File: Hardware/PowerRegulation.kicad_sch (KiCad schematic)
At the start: 43 parts, among them Q3 AO3401A, U13 TPS54332DDA, U14 AMS1117-3.3, U15 RT9193-33GB, U8 STUSB4500QTR

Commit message: further clean up, switch to desktop
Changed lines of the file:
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@@
 		(end 170.18 190.5)
 		(stroke
-			(width 0.254)
+			(width 0.1778)
 			(type solid)
 		)
@@
 	(text "Indicator LEDs\n"
 		(exclude_from_sim no)
-		(at 204.216 23.622 0)
+		(at 203.454 23.622 0)
 		(effects
 			(font
@@
 	(text "Testpoints"
 		(exclude_from_sim no)
-		(at 205.74 73.66 0)
+		(at 200.152 73.66 0)
 		(effects
 			(font

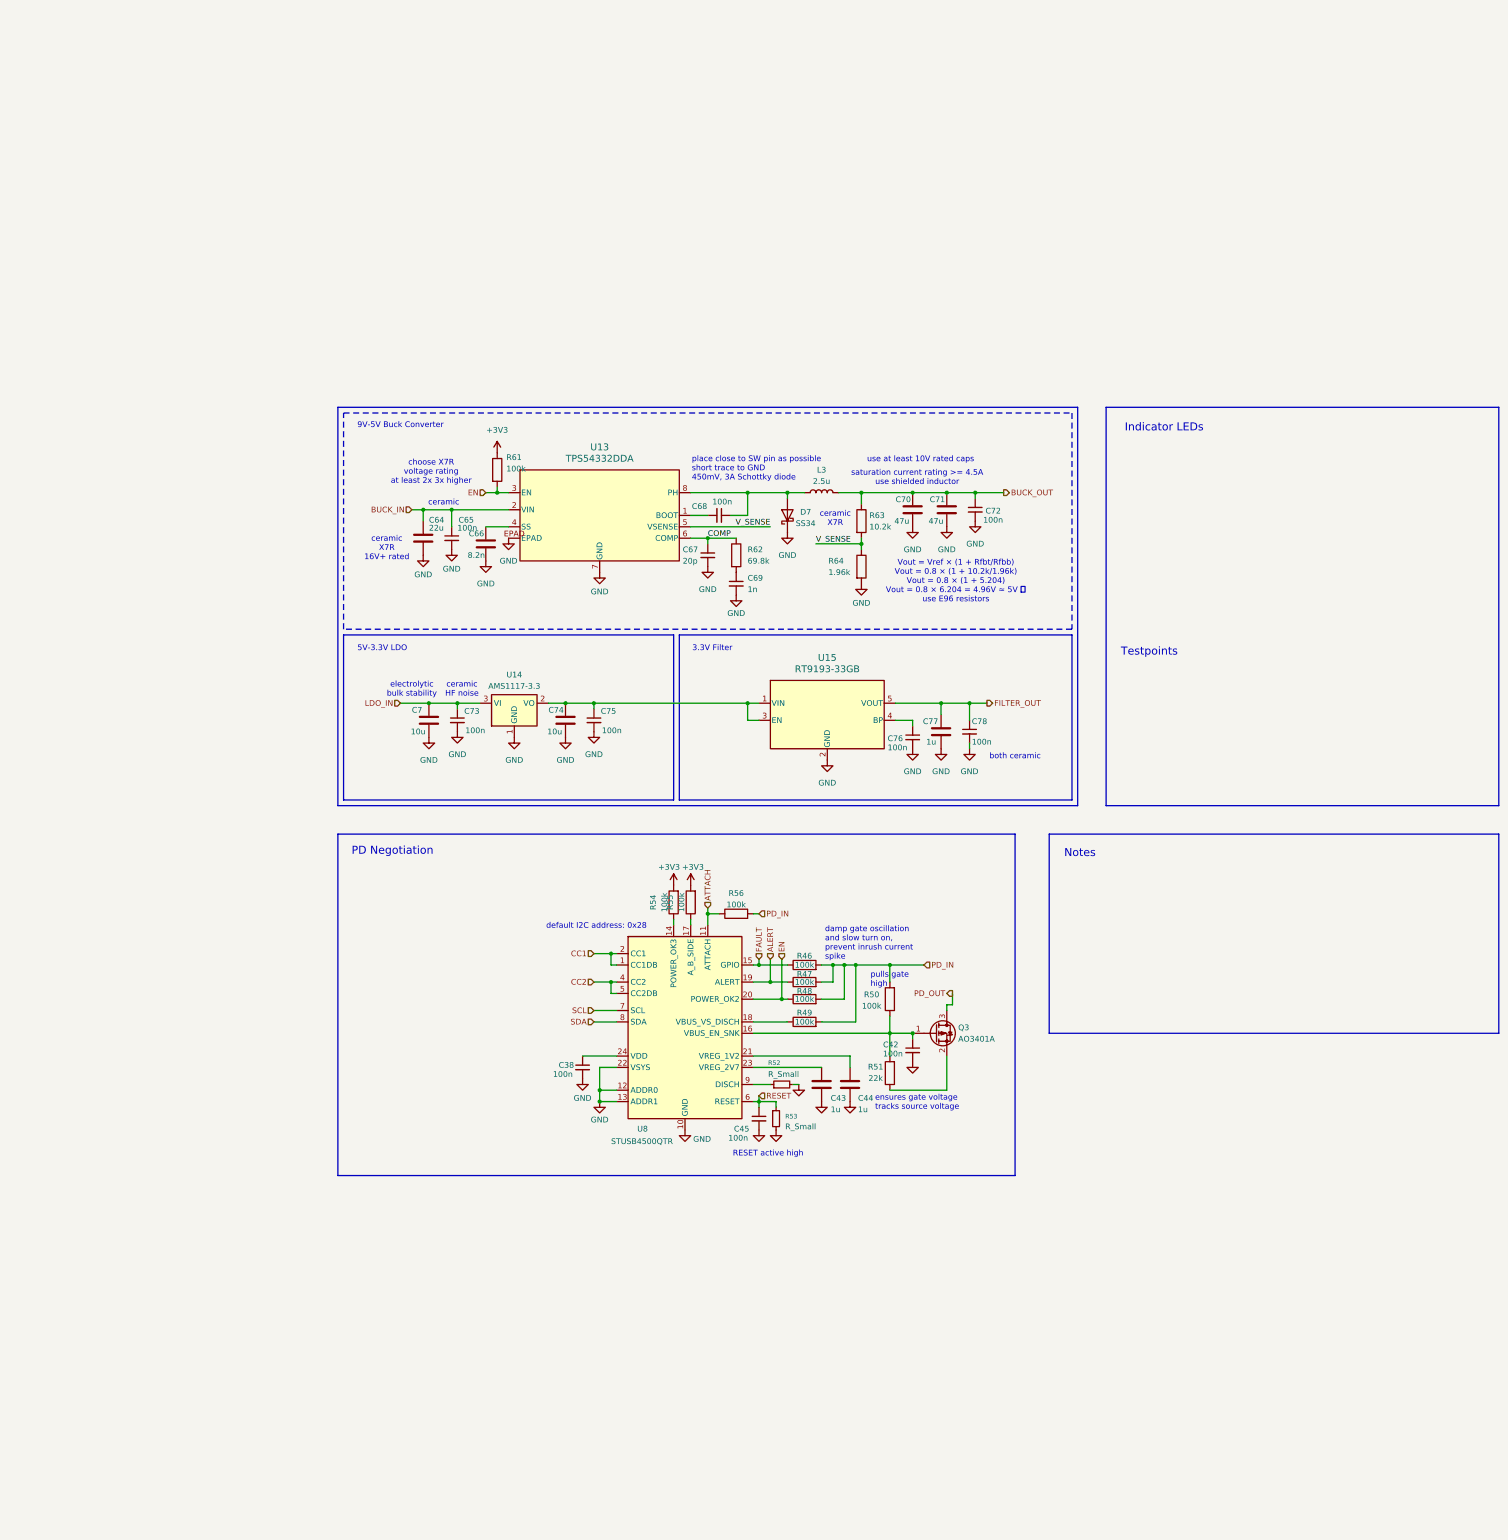
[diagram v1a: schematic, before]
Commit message: new buck ic with 6A current limit, more organization and changes
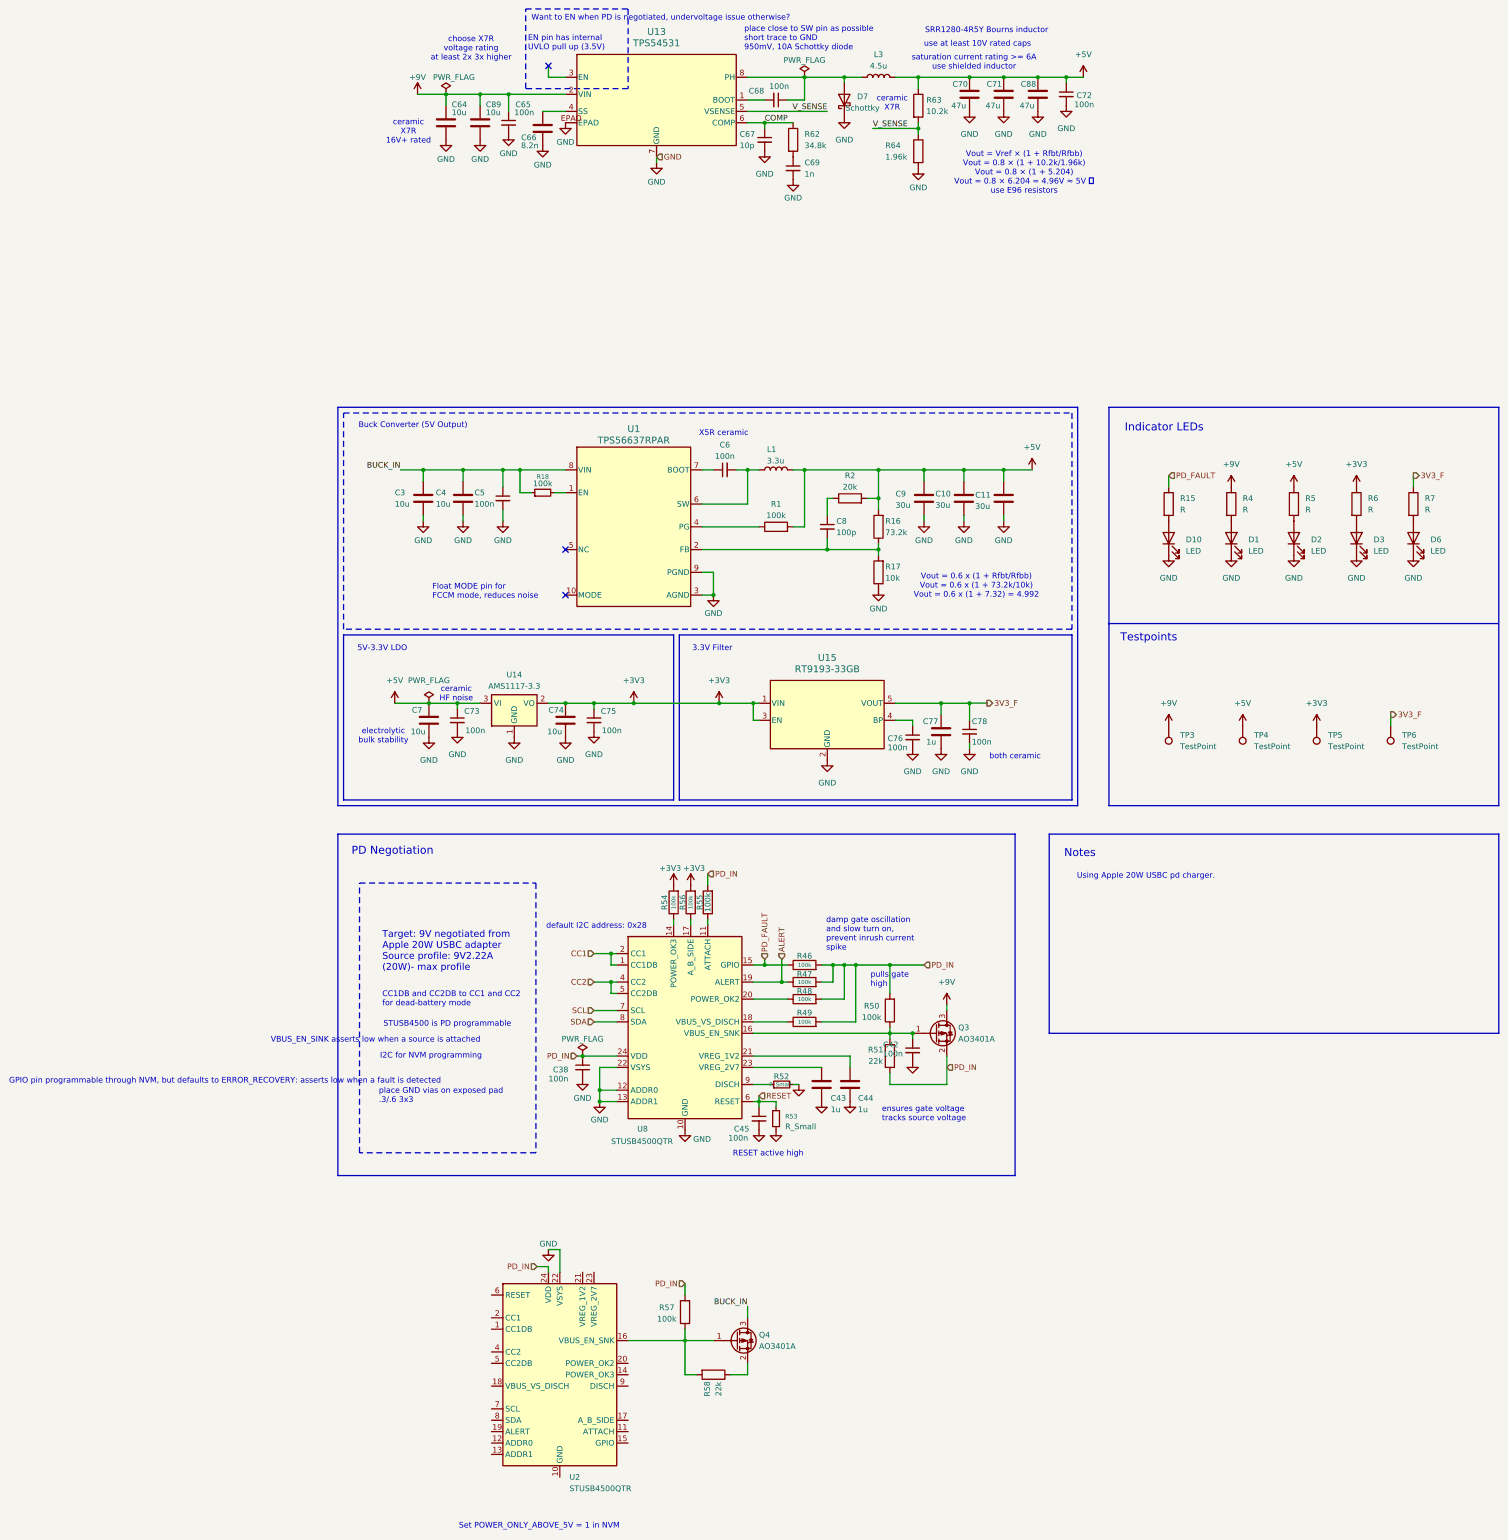
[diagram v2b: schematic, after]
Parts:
- removed R61: 100k, symbol Device:R
- added C10, C11, C9: 30u, Capacitor_SMD:C_1210_3225Metric_Pad1.33x2.70mm_HandSolder, symbol Device:C
- added C3, C4: 10u, Capacitor_SMD:C_0805_2012Metric_Pad1.18x1.45mm_HandSolder, symbol Device:C
- added C5: 100n, Capacitor_SMD:C_0603_1608Metric_Pad1.08x0.95mm_HandSolder, symbol Device:C_Small
- added C6: 100n, Capacitor_SMD:C_0805_2012Metric_Pad1.18x1.45mm_HandSolder, symbol Device:C_Small
- added C8: 100p, Capacitor_SMD:C_0201_0603Metric_Pad0.64x0.40mm_HandSolder, symbol Device:C_Small
- added C88: 47u, Capacitor_SMD:C_1210_3225Metric_Pad1.33x2.70mm_HandSolder, symbol Device:C
- added C89: 10u, Capacitor_SMD:C_1210_3225Metric_Pad1.33x2.70mm_HandSolder, symbol Device:C
- added D1, D10, D2, D3, D6: LED, symbol Device:LED
- added L1: 3.3u, symbol Device:L
- added Q4: AO3401A, Package_TO_SOT_SMD:SOT-23, symbol Transistor_FET:AO3401A
- added R1, R57: 100k, symbol Device:R
- added R15, R4, R5, R6, R7: R, symbol Device:R
- added R16: 73.2k, symbol Device:R
- added R17: 10k, symbol Device:R
- added R18: 100k, symbol Device:R_Small
- added R2: 20k, symbol Device:R
- added R58: 22k, symbol Device:R
- added TP3, TP4, TP5, TP6: TestPoint, symbol Connector:TestPoint
- added U1: TPS56637RPAR, RPA0010A, symbol LED Sign:TPS56637RPAR
- added U2: STUSB4500QTR, Package_DFN_QFN:QFN-24-1EP_4x4mm_P0.5mm_EP2.7x2.7mm, symbol Interface_USB:STUSB4500QTR
- C64: value 22u -> 10u; footprint (none) -> Capacitor_SMD:C_1210_3225Metric_Pad1.33x2.70mm_HandSolder; P/N (none) -> MSASU32MSB5106KPNA01
- C66: footprint (none) -> Capacitor_SMD:C_0201_0603Metric_Pad0.64x0.40mm_HandSolder; P/N (none) -> GRM033R71A822KA01D
- C67: value 20p -> 10p; footprint (none) -> Capacitor_SMD:C_0805_2012Metric_Pad1.18x1.45mm_HandSolder; P/N (none) -> CC0805JRNPO9BN100
- C68: footprint (none) -> Capacitor_SMD:C_0805_2012Metric_Pad1.18x1.45mm_HandSolder; P/N (none) -> 08053C104KAT2A
- C69: footprint (none) -> Capacitor_SMD:C_0402_1005Metric_Pad0.74x0.62mm_HandSolder; P/N (none) -> GRM1555C1H102JA01J
- C70, C71: footprint (none) -> Capacitor_SMD:C_1210_3225Metric_Pad1.33x2.70mm_HandSolder; P/N (none) -> GRM32ER61C476KE15L
- D7: value SS34 -> Schottky; P/N (none) -> SBRD10200TR
- L3: value 2.5u -> 4.5u; P/N (none) -> SRR1280-4R5Y
- R62: value 69.8k -> 34.8k; P/N (none) -> CRCW040234K8FKED
- R63: P/N (none) -> CRCW040210K2FKED
- R64: P/N (none) -> CRCW04021K96FKED
- U13: value TPS54332DDA -> TPS54531
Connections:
- net LDO_IN is gone; now on net +5V: C7.1, C73.1, U14.3 (VI)
- net +3V3: now also C74.1, C75.1, U14.2 (VO), U15.1 (VIN), U15.3 (EN), R6.1, TP5.1
- net BUCK_IN: now also C3.1, C4.1, C5.1, Q4.3 (D), R18.1, U1.8 (VIN); no longer C64.1, C65.1, U13.2 (VIN)
- net GND: now also C10.2, C11.2, C3.2, C4.2, C5.2, C88.2, C89.2, C9.2, D1.1 (K), D10.1 (K), D2.1 (K), D3.1 (K), D6.1 (K), R17.1, U1.3 (AGND), U1.9 (PGND), U2.22 (VSYS)
- net PD_IN: now also C38.1, Q3.2 (S), R51.1, U8.24 (VDD), R57.2, U2.24 (VDD)
- net ATTACH: no longer names the net of R56.1, U8.11 (ATTACH)
- net BUCK_OUT renamed +5V
- net +5V: now also C10.1, C11.1, C88.1, C9.1, L1.2, R1.2, R16.2, R2.2, R5.1, TP4.1
- net EN: no longer names the net of R48.1, U8.20 (POWER_OK2)
- net EN: no longer U13.3 (EN)
- net FAULT renamed PD_FAULT
- net PD_FAULT: now also R15.1
- net FILTER_OUT renamed 3V3_F
- net 3V3_F: now also R7.1, TP6.1
- net PD_OUT renamed +9V
- net +9V: now also C64.1, C65.1, U13.2 (VIN), C89.1, R4.1, TP3.1
- new net: C6.2, L1.1, U1.6 (SW)
- new net: U2.10 (GND), U2.25 (GND)
- new net: Q4.1 (G), R57.1, R58.2, U2.16 (VBUS_EN_SNK)
- new net: C6.1, U1.7 (BOOT)
- new net: R18.2, U1.1 (EN)
- new net: C8.2, R16.1, R17.2, U1.2 (FB)
- new net: R1.1, U1.4 (PG)
- new net: D6.2 (A), R7.2
- new net: D10.2 (A), R15.2
- new net: C8.1, R2.1
- new net: D1.2 (A), R4.2
- new net: D3.2 (A), R6.2
- new net: D2.2 (A), R5.2
- new net: Q4.2 (S), R58.1
- no-connect marks 0 -> 3
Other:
- note added: "Buck Converter (5V Output)"
- note added: "CC1DB and CC2DB to CC1 and CC2 for dead-battery mode"
- note added: "EN pin has internal UVLO pull up (3.5V)"
- note added: "Float MODE pin for FCCM mode, reduces noise"
- note added: "GPIO pin programmable through NVM, but defaults to ERROR_RECOVERY: asserts low when a fault is detected"
- note added: "I2C for NVM programming"
- note added: "SRR1280-4R5Y Bourns inductor"
- note added: "STUSB4500 is PD programmable"
- note added: "Set POWER_ONLY_ABOVE_5V = 1 in NVM"
- note added: "Target: 9V negotiated from Apple 20W USBC adapter Source profile: 9V2.22A (20W)- max profile"
- note added: "Using Apple 20W USBC pd charger."
- note added: "VBUS_EN_SINK asserts low when a source is attached"
- note added: "Vout = 0.6 x (1 + Rfbt/Rfbb) Vout = 0.6 x (1 + 73.2k/10k) Vout = 0.6 x (1 + 7.32) = 4.992"
- note added: "Want to EN when PD is negotiated, undervoltage issue otherwise?"
- note added: "X5R ceramic"
- note added: "place GND vias on exposed pad .3/.6 3x3"
- note added: "place close to SW pin as possible short trace to GND 950mV, 10A Schottky diode"
- note added: "saturation current rating >= 6A use shielded inductor"
- note removed: "9V-5V Buck Converter"
- note removed: "ceramic"
- note removed: "place close to SW pin as possible short trace to GND 450mV, 3A Schottky diode"
- note removed: "saturation current rating >= 4.5A use shielded inductor"
- moved on the sheet: C64, C65, C66, C67, C68, C69, C70, C71, C72, D7, L3, R50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

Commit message: revise pd controller
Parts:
- removed C64, C89: 10u, Capacitor_SMD:C_1210_3225Metric_Pad1.33x2.70mm_HandSolder, symbol Device:C
- removed C65, C72: 100n, symbol Device:C_Small
- removed C66: 8.2n, Capacitor_SMD:C_0201_0603Metric_Pad0.64x0.40mm_HandSolder, symbol Device:C
- removed C67: 10p, Capacitor_SMD:C_0805_2012Metric_Pad1.18x1.45mm_HandSolder, symbol Device:C_Small
- removed C68: 100n, Capacitor_SMD:C_0805_2012Metric_Pad1.18x1.45mm_HandSolder, symbol Device:C_Small
- removed C69: 1n, Capacitor_SMD:C_0402_1005Metric_Pad0.74x0.62mm_HandSolder, symbol Device:C_Small
- removed C70, C71, C88: 47u, Capacitor_SMD:C_1210_3225Metric_Pad1.33x2.70mm_HandSolder, symbol Device:C
- removed D7: Schottky, Diode_SMD:D_SMA, symbol Diode:SS34
- removed L3: 4.5u, symbol Device:L
- removed U13: TPS54531, DDA8_3X2P13, symbol LED Sign:TPS54332DDA
- added C46: 100n, symbol Device:C_Small
- added C47, C48: 1u, symbol Device:C_Small
- added R59: 100, symbol Device:R_Small
- added R61: 100k, symbol Device:R_Small
- added R75, R76, R77, R78: 100k, symbol Device:R
- R62: value 34.8k -> 100k; P/N CRCW040234K8FKED -> (none)
- R63: value 10.2k -> 100k; P/N CRCW040210K2FKED -> (none)
- R64: value 1.96k -> 100k; P/N CRCW04021K96FKED -> (none)
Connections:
- net COMP is gone; now on net PD_IN: R62.1
- net V_SENSE is gone; now on net PD_IN: R63.2, R64.1
- net +3V3: now also R76.2, R78.2
- net +5V: no longer R63.1
- net CC1: now also U2.1 (CC1DB), U2.2 (CC1)
- net CC2: now also U2.4 (CC2), U2.5 (CC2DB)
- net GND: now also U2.10 (GND), U2.12 (ADDR0), U2.13 (ADDR1), U2.25 (GND), C46.2, C47.1, C48.1, R59.2, R61.2; no longer R64.2
- net PD_IN: now also R75.2, R77.2
- net RESET: now also U2.6 (RESET), C46.1, R61.1
- net SCL: now also U2.7 (SCL)
- net SDA: now also U2.8 (SDA)
- net at U2.11 (ATTACH): now also R63.1
- net at U2.14 (POWER_OK3): now also R78.1
- net at U2.15 (GPIO): now also R62.2
- net at U2.17 (A_B_SIDE): now also R76.1
- net at U2.18 (VBUS_VS_DISCH): now also R64.2
- net at U2.19 (ALERT): now also R75.1
- net at U2.20 (POWER_OK2): now also R77.1
- net at U2.21 (VREG_1V2): now also C47.2
- net at U2.23 (VREG_2V7): now also C48.2
- net at U2.9 (DISCH): now also R59.1
- no-connect marks 3 -> 2
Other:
- note added: "caps rated ideally >30V"
- note added: "chip off during initial NVM programming"
- note removed: "EN pin has internal UVLO pull up (3.5V)"
- note removed: "SRR1280-4R5Y Bourns inductor"
- note removed: "Using Apple 20W USBC pd charger."
- note removed: "Vout = Vref × (1 + Rfbt/Rfbb) Vout = 0.8 × (1 + 10.2k/1.96k) Vout = 0.8 × (1 + 5.204) Vout = 0.8 × 6.204 = 4.96V ≈ 5V ✅ use E96 resistors"
- note removed: "Want to EN when PD is negotiated, undervoltage issue otherwise?"
- note removed: "ceramic X7R"
- note removed: "ceramic X7R 16V+ rated"
- note removed: "choose X7R voltage rating at least 2x 3x higher"
- note removed: "place close to SW pin as possible short trace to GND 950mV, 10A Schottky diode"
- note removed: "saturation current rating >= 6A use shielded inductor"
- note removed: "use at least 10V rated caps"
- moved on the sheet: C38, C42, C43, C44, C45, Q3, Q4, R18, R46, R47, R48, R49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
